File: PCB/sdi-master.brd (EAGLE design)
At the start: 71 x 18.6 mm, 21 parts, among them J4 POWER_JACKPTH_LOCK, U1 ATSAMD11C14A-SSUT, U3 LDL1117S12R

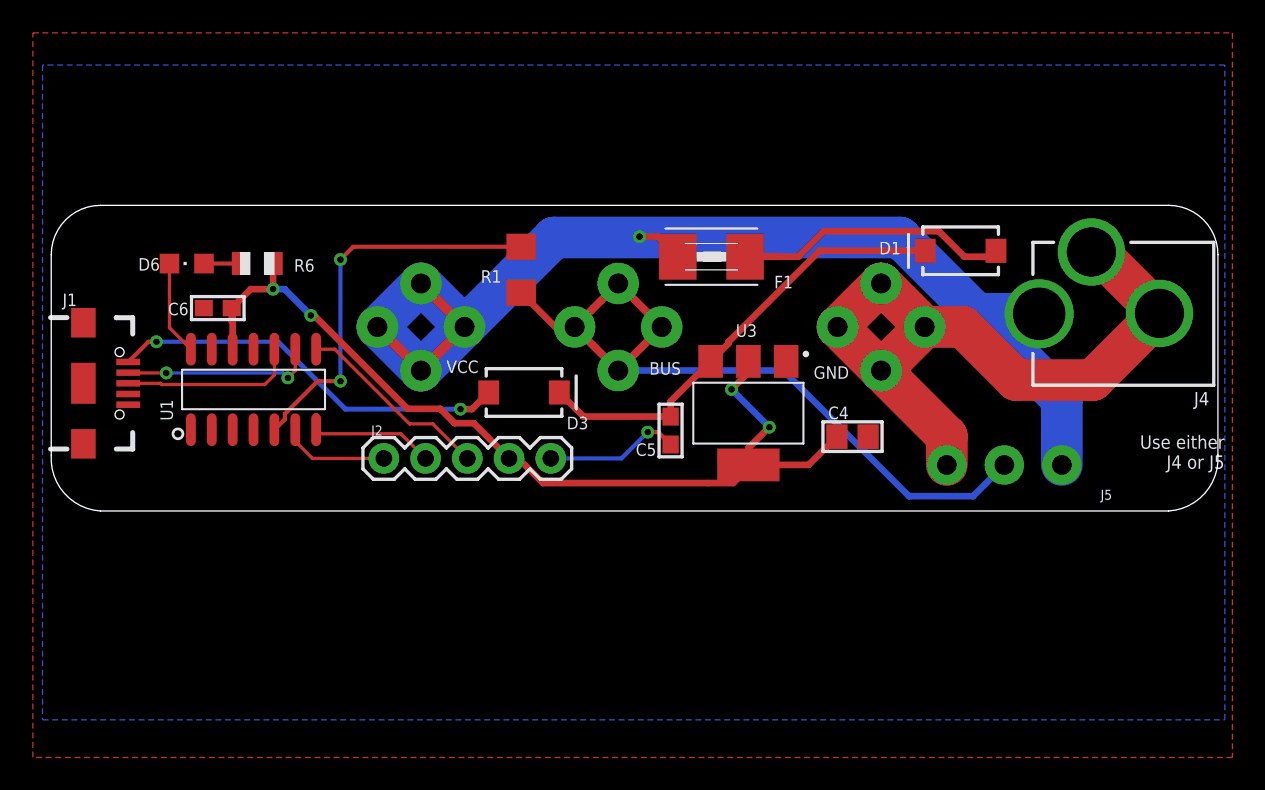
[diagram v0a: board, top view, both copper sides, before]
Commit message: added 4pin connector for remaining pins on all boards
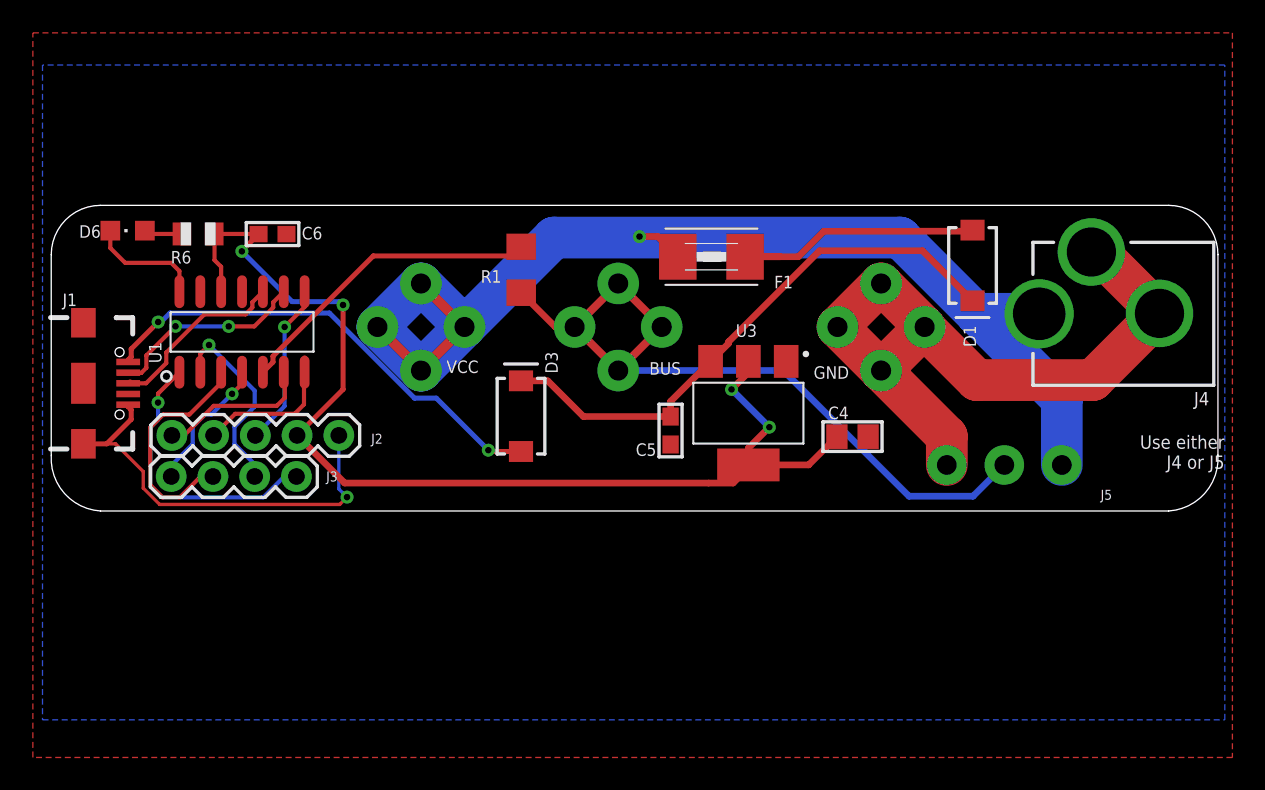
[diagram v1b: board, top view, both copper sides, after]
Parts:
- added J3: (no value), SparkFun-Connectors:1X04
- moved J2 13.0 mm to (17.5, 13.4)
- moved C6 5.60 mm to (13.5, 25.7), turned to 0 degrees
- moved D6 4.12 mm to (4.65, 25.9)
- moved R6 4.02 mm to (8.94, 25.7)
- moved U1 3.57 mm to (11.6, 19.7)
- moved D3 1.45 mm to (28.6, 14.6), turned to 90 degrees
- moved D1 1.15 mm to (56.1, 23.7), turned to 270 degrees
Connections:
- new net N$1: J3.4, U1.1
- new net N$2: J3.3, U1.2
- new net N$3: J3.2, U1.3
- new net N$7: J3.1, U1.4
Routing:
- net GND: track 53.7 -> 72.2 mm
- net N$1: track 0.00 -> 17.3 mm, vias 0 -> 1
- net N$3: track 0.00 -> 15.6 mm
- net N$2: track 0.00 -> 12.0 mm, vias 0 -> 1
- net 3.3V: track 59.4 -> 71.2 mm
- net N$7: track 0.00 -> 8.36 mm, vias 0 -> 1
- net VCC: track 27.7 -> 34.4 mm
- net N$5: track 24.2 -> 19.1 mm, vias 2 -> 0
- net N$4: track 24.6 -> 29.0 mm
- net RESET: track 6.52 -> 9.40 mm
- net N$12: track 18.9 -> 16.7 mm
- net 04: track 5.75 -> 7.61 mm
- net SWDIO: track 12.0 -> 10.5 mm, vias 0 -> 1
- net SWCLK: track 8.26 -> 9.13 mm
- net USB+: track 10.7 -> 11.2 mm

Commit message: modified sdi master to suit sdi application node
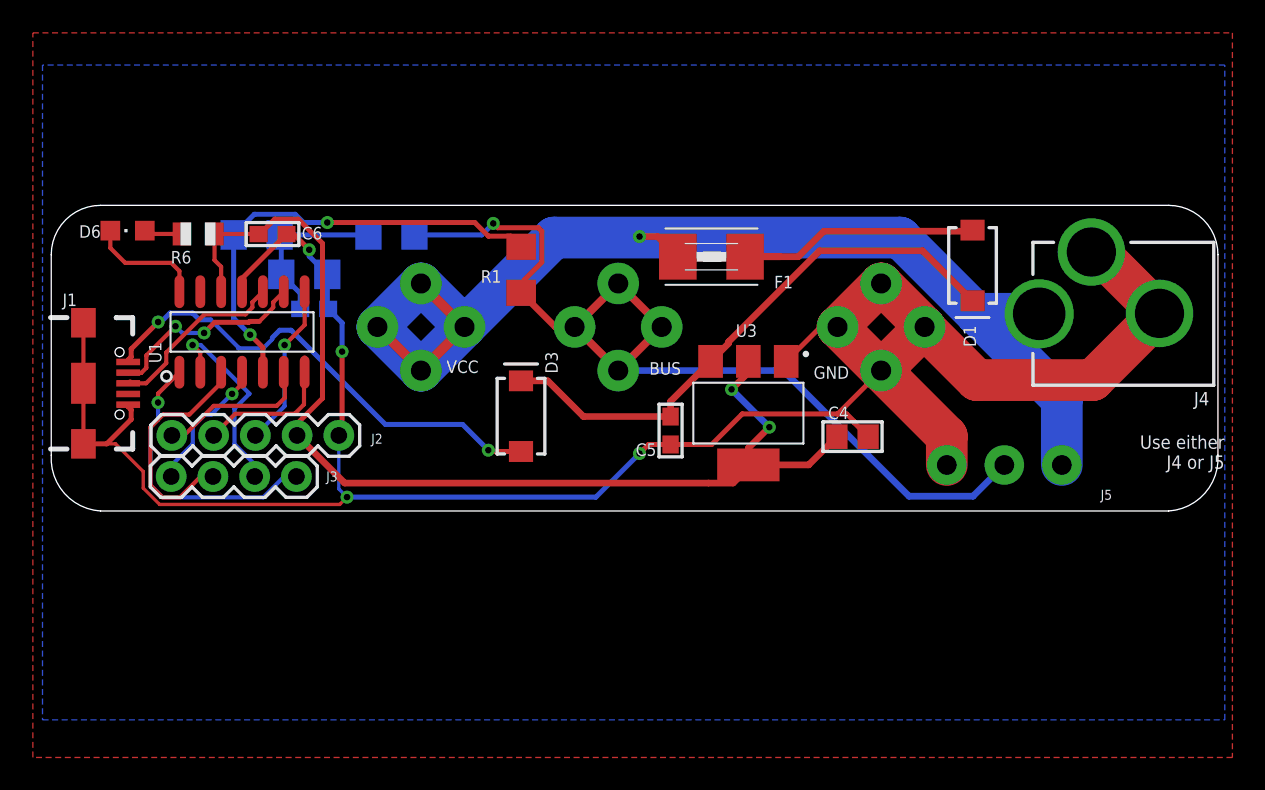
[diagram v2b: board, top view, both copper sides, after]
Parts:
- added C20: 3.3nF, microbuilder:0603
- added R20: 200k, SparkFun-Resistors:1206
- added R21, R22: 510R, SparkFun-Resistors:1206
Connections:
- new net N$8: C20.1, R20.2, R21.1, R22.2
- net BUS: now also R22.1
- net GND: now also C20.2, R20.1
- net N$5: now also R21.2
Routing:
- net GND: track 72.2 -> 140.4 mm, vias 1 -> 4
- net BUS: track 46.7 -> 59.3 mm, vias 0 -> 1
- net N$8: track 0.00 -> 11.0 mm
- net N$5: track 19.1 -> 28.7 mm, vias 0 -> 2
- net N$4: track 29.0 -> 30.0 mm
- net 3.3V: track 71.2 -> 70.3 mm, vias 4 -> 2

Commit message: unknown changes, break has been too long
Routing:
- net BUS: track 59.3 -> 54.7 mm
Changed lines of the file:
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@@
 <?xml version="1.0" encoding="utf-8"?>
 <!DOCTYPE eagle SYSTEM "eagle.dtd">
-<eagle version="9.2.2">
+<eagle version="9.3.0">
 <drawing>
 <settings>
-<setting alwaysvectorfont="yes"/>
+<setting alwaysvectorfont="no"/>
 <setting keepoldvectorfont="yes"/>
 <setting verticaltext="up"/>
@@
 <wire x1="52.2" y1="9.7" x2="56.1" y2="9.7" width="0.4064" layer="16"/>
 <contactref element="R22" pad="1"/>
-<wire x1="22.1" y1="25.6" x2="26.2" y2="25.6" width="0.3048" layer="16"/>
-<wire x1="26.2" y1="25.6" x2="26.9" y2="26.3" width="0.3048" layer="16"/>
-<via x="26.9" y="26.3" extent="1-16" drill="0.3937"/>
-<wire x1="29.64529375" y1="26.0356" x2="29.8536" y2="25.82729375" width="0.3048" layer="1"/>
-<wire x1="29.8536" y1="25.82729375" x2="29.8536" y2="23.93270625" width="0.3048" layer="1"/>
-<wire x1="26.9" y1="26.3" x2="27.1644" y2="26.0356" width="0.3048" layer="1"/>
-<wire x1="28.789" y1="22.86810625" x2="28.789" y2="21.889" width="0.3048" layer="1"/>
-<wire x1="27.1644" y1="26.0356" x2="29.64529375" y2="26.0356" width="0.3048" layer="1"/>
-<wire x1="29.8536" y1="23.93270625" x2="28.789" y2="22.86810625" width="0.3048" layer="1"/>
+<wire x1="22.1" y1="25.6" x2="23.9" y2="25.6" width="0.3048" layer="16"/>
+<wire x1="28.598" y1="22.08" x2="25.078" y2="25.6" width="0.3048" layer="1"/>
+<wire x1="25.078" y1="25.6" x2="23.9" y2="25.6" width="0.3048" layer="1"/>
+<via x="23.9" y="25.6" extent="1-16" drill="0.3937"/>
 </signal>
 <signal name="N$6">
